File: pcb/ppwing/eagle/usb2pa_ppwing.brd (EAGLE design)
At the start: 85.1 x 68.6 mm, 54 parts, among them Q1 24 MHz, SW1 EVQQ2, U2 LM3525-H, U3 INA219AID

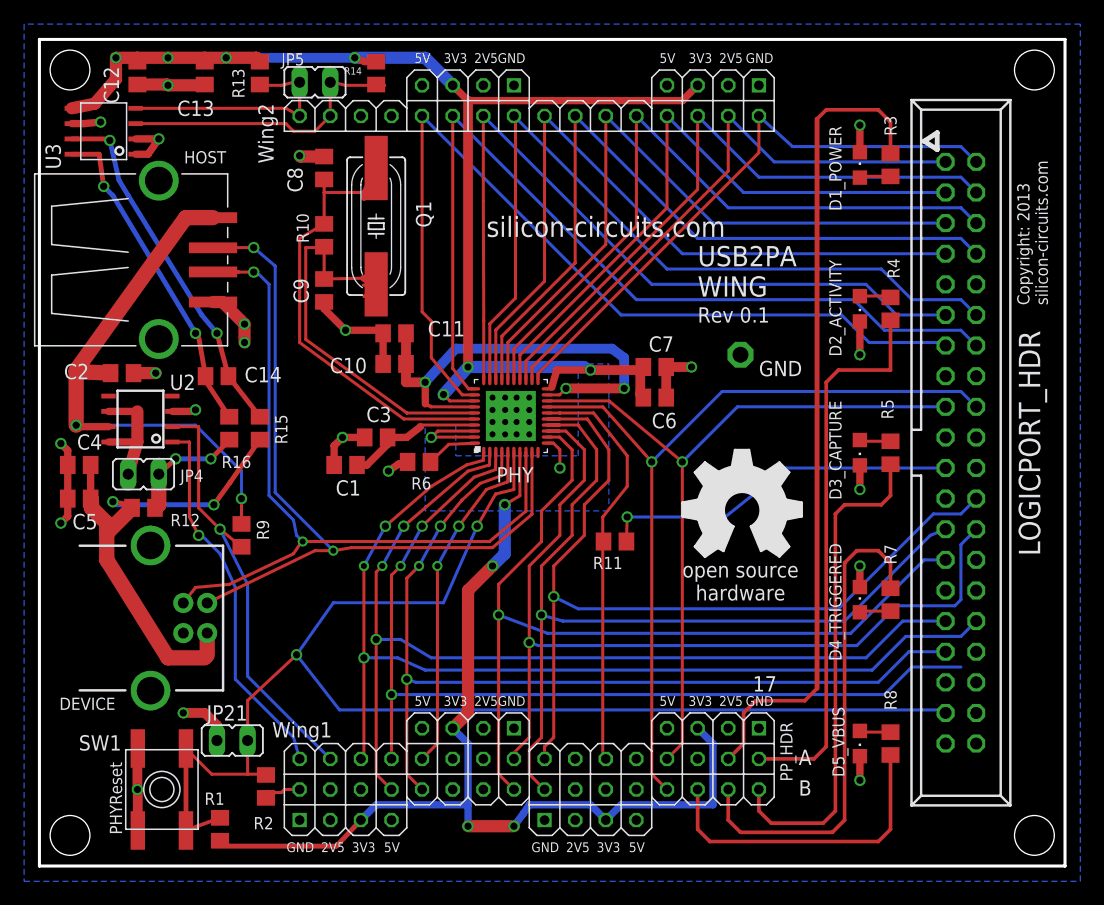
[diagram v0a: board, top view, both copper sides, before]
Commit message: REV0P1a : This is what was actually submitted to the board shop.
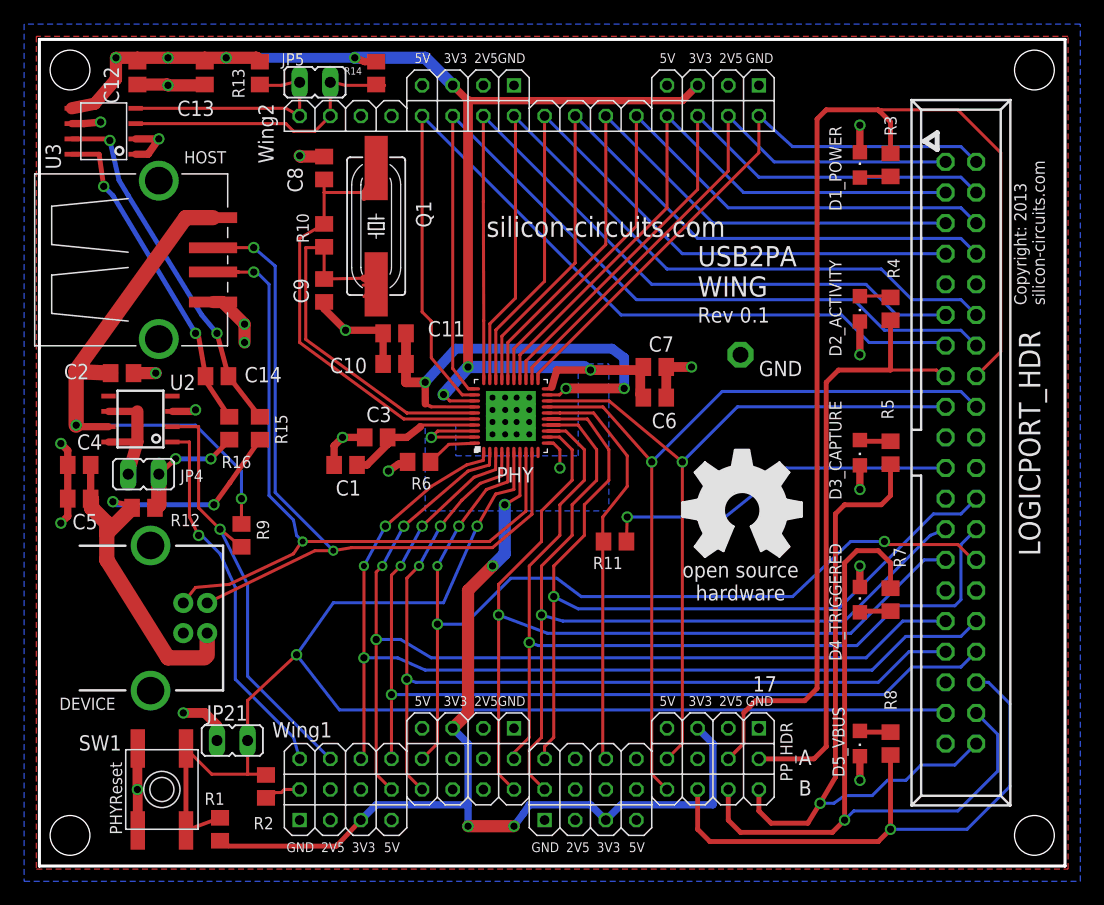
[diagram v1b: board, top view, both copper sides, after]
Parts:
- moved CC_LICENSE 0.72 mm to (63.2, 63.9)
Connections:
- net GND: now also LOGICPORT_HDR.29
- net LED1: now also LOGICPORT_HDR.16
- net LED2: now also LOGICPORT_HDR.15
- net LED3: now also LOGICPORT_HDR.40
- net LED4: now also LOGICPORT_HDR.38
- net LED5: now also LOGICPORT_HDR.36
- net TXREADY: now also LOGICPORT_HDR.34
- net TXVALID: now also LOGICPORT_HDR.28
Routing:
- net TXVALID: track 28.4 -> 77.7 mm, vias 2 -> 4
- net LED1: track 68.0 -> 98.9 mm
- net LED5: track 26.3 -> 48.1 mm, vias 0 -> 1
- net LED4: track 41.1 -> 61.1 mm, vias 0 -> 1
- net LED3: track 41.4 -> 55.3 mm, vias 0 -> 1
- net LED2: track 46.1 -> 50.9 mm
- net TXREADY: track 77.5 -> 79.3 mm
- added copper zone on layer 1, net N$2
